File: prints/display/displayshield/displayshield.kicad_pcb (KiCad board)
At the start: 2 copper layers, 9 parts, among them J1 Conn_01x16, J2 Screw_Terminal_01x11, SW1 SW_Push

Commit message: Finished Displayshield Print
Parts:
- added G***: LOGO, logo:Skógahöf_S, F.Cu at (182.1, 113.7)
- moved BZ1 128.9 mm to (162.3, 113.7)
- moved D1 116.4 mm to (180.5, 79.7)
- moved J2 107.8 mm to (124.1, 115.2), turned to 90 degrees
- moved SW1 106.4 mm to (145.6, 112.2)
- moved J1 99.1 mm to (133.6, 79.7), turned to 90 degrees
- moved RV1 98.7 mm to (137.6, 113.6)
- moved R3 97.5 mm to (140.1, 109.7)
- moved R2 96.3 mm to (136.1, 109.7)
- moved R1 95.5 mm to (132.1, 109.7)
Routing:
- net GND: track 0.00 -> 157.5 mm
- net Net-(J2-Pin_9): track 0.00 -> 147.6 mm
- net +5V: track 0.00 -> 139.3 mm
- net Net-(BZ1-+): track 0.00 -> 103.4 mm
- net Net-(J1-Pin_14): track 0.00 -> 88.0 mm
- net Net-(J1-Pin_13): track 0.00 -> 77.7 mm
- net Net-(J1-Pin_12): track 0.00 -> 70.1 mm
- net Net-(J1-Pin_6): track 0.00 -> 69.7 mm
- net Net-(J1-Pin_11): track 0.00 -> 62.3 mm
- net Net-(J2-Pin_11): track 0.00 -> 59.1 mm
- net Net-(D1-A): track 0.00 -> 54.4 mm
- net Net-(J1-Pin_15): track 0.00 -> 50.5 mm
- net Net-(J1-Pin_3): track 0.00 -> 48.1 mm
- net Net-(J1-Pin_4): track 0.00 -> 24.9 mm
- net (no net): vias 0 -> 4
- added copper zone on B.Cu, net GND
- added copper zone on F.Cu, net GND
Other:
- board outline added: 80 x 52 mm
- board text added: "PREN2: Skógahöf DisplayShield"
- board text added: "Revision 1.0"

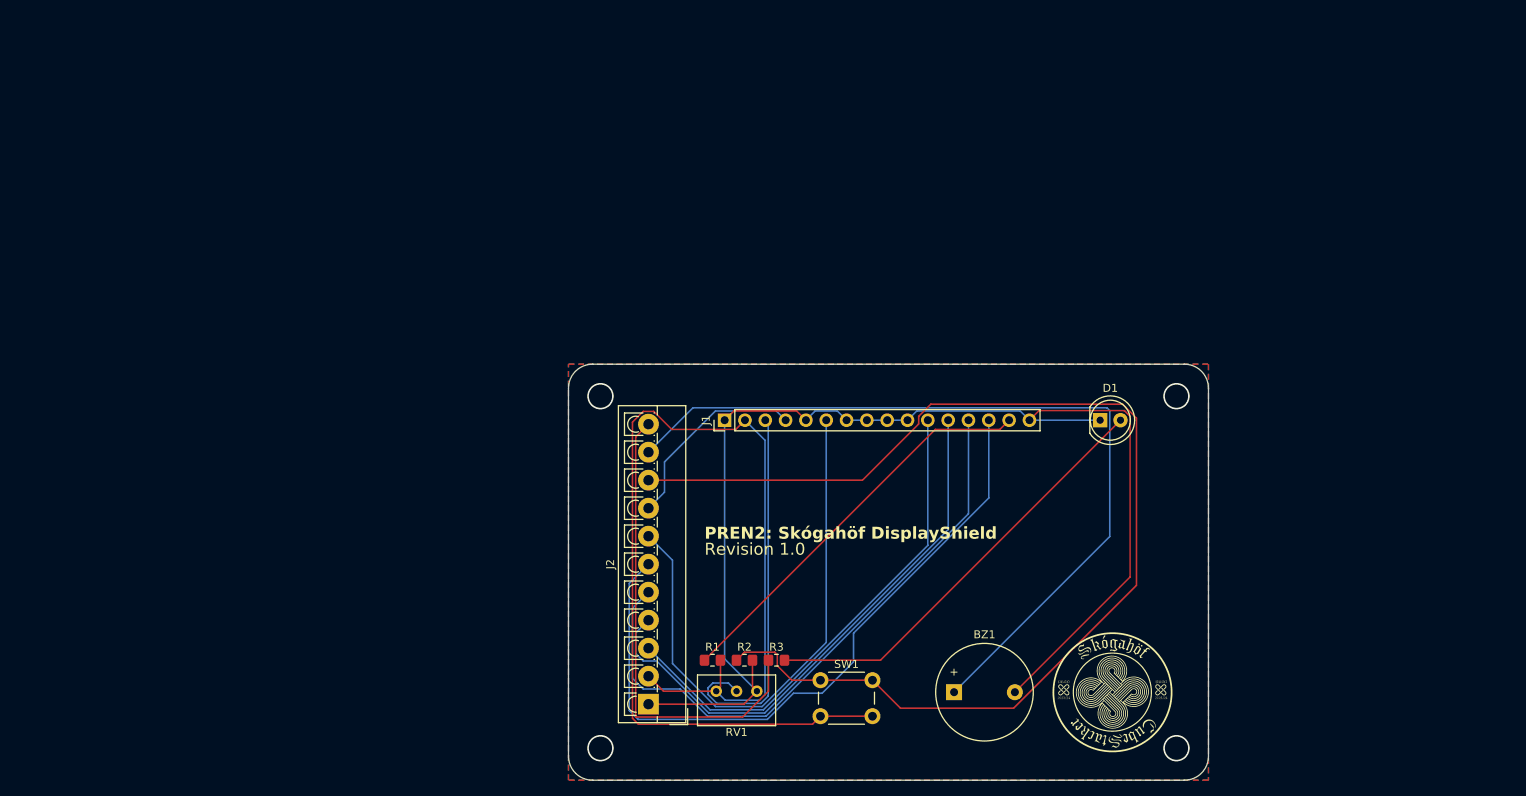
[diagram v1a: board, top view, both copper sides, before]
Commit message: added new Printfiles for Displayshield and Measurements for second stack
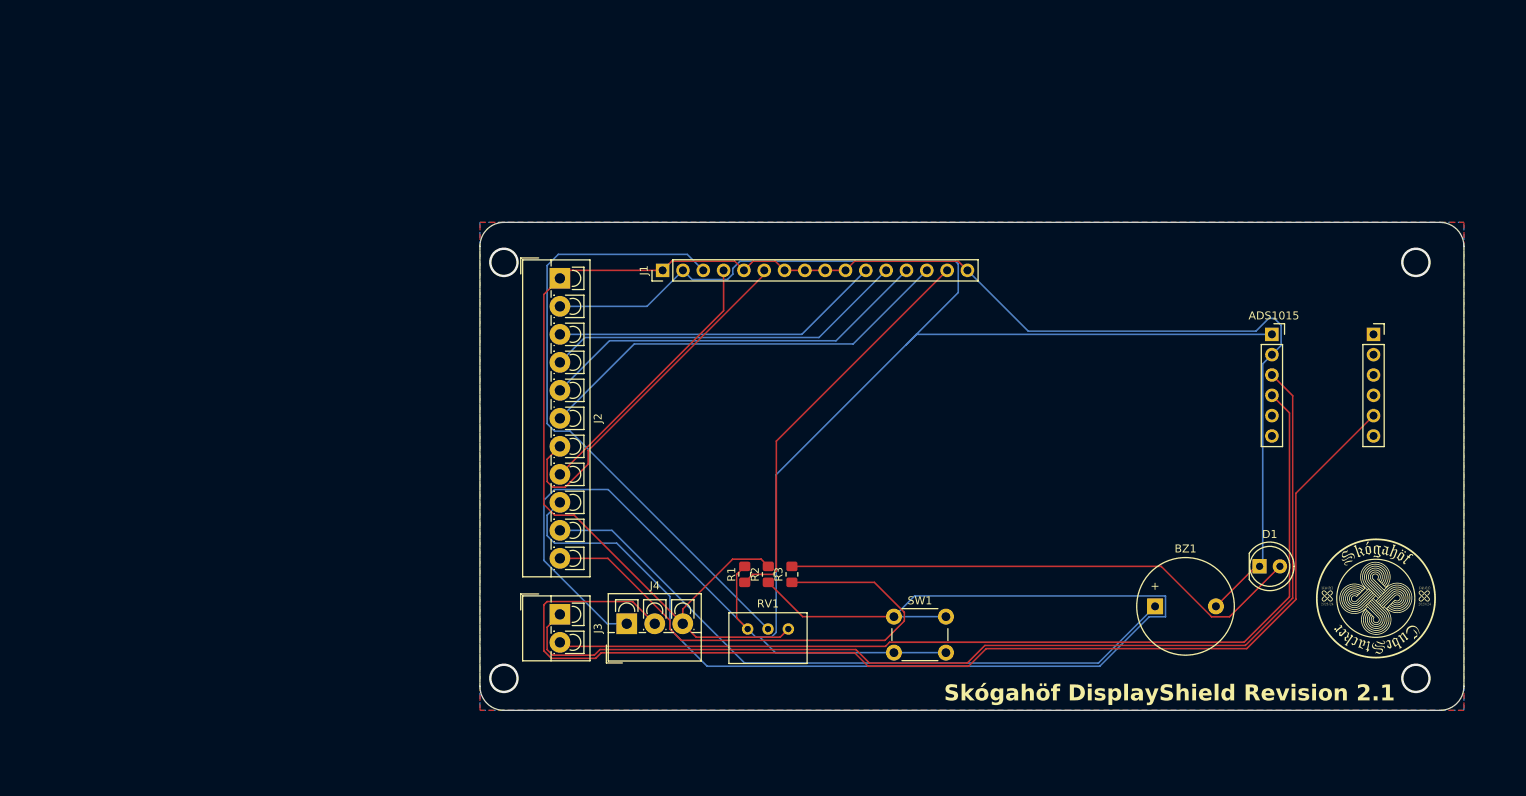
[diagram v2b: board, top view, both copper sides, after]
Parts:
- added ADS1015: ~, ADAFRUIT:ADS1015, F.Cu at (208.7, 73.2)
- added J3: RaspberryPiADC, TerminalBlock_4Ucon:TerminalBlock_4Ucon_1x02_P3.50mm_Vertical, F.Cu at (113.0, 104.0)
- added J4: CurrentSensor, TerminalBlock_4Ucon:TerminalBlock_4Ucon_1x03_P3.50mm_Vertical, F.Cu at (121.4, 105.2)
- J1: value Conn_01x16 -> Display
- J2: value Screw_Terminal_01x11 -> RaspberryPiDisplay
- moved J2 54.4 mm to (113.0, 62.0), turned to -90 degrees
- moved G*** 35.0 mm to (215.0, 102.0)
- moved BZ1 27.3 mm to (187.4, 103.0)
- moved D1 27.0 mm to (200.5, 98.0)
- moved J1 20.3 mm to (125.8, 61.0)
- moved SW1 12.1 mm to (154.8, 104.3)
- moved R1 11.5 mm to (136.1, 99.0), turned to 90 degrees
- moved R2 11.1 mm to (139.1, 99.0), turned to 90 degrees
- moved R3 10.9 mm to (142.0, 99.0), turned to 90 degrees
- moved RV1 8.71 mm to (141.6, 105.8)
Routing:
- net Net-(ADS1015-A0): track 0.00 -> 146.8 mm
- net Net-(ADS1015-SCL): track 0.00 -> 131.9 mm
- net Net-(ADS1015-SDA): track 0.00 -> 120.1 mm
- net +5V: track 139.3 -> 246.9 mm
- net GND: track 157.5 -> 218.8 mm
- net Net-(J1-Pin_14): track 88.0 -> 53.5 mm
- net Net-(J1-Pin_3): track 48.1 -> 78.9 mm
- net Net-(J1-Pin_13): track 77.7 -> 49.5 mm
- net Net-(J1-Pin_6): track 69.7 -> 45.0 mm
- net Net-(J1-Pin_12): track 70.1 -> 45.5 mm
- net Net-(J1-Pin_11): track 62.3 -> 41.6 mm
- net Net-(BZ1-+): track 103.4 -> 84.2 mm
- net Net-(D1-A): track 54.4 -> 66.2 mm
- net Net-(J1-Pin_4): track 24.9 -> 34.0 mm
- net Net-(J2-Pin_9): track 147.6 -> 155.4 mm
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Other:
- board size 80 x 52 mm -> 123 x 61 mm
- board text added: "Skógahöf DisplayShield Revision 2.1"
- board text removed: "PREN2: Skógahöf DisplayShield"
- board text removed: "Revision 1.0"

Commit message: updated StackMeasurements
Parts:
- moved ADS1015 2.69 mm to (211.4, 73.2)
- moved J2 2.69 mm to (115.7, 62.0)
- moved J3 2.69 mm to (115.7, 104.0)
- moved J4 2.69 mm to (124.0, 105.2)
- moved BZ1 2.69 mm to (190.1, 103.0)
- moved D1 2.69 mm to (203.2, 98.0)
- moved J1 2.69 mm to (128.5, 61.0)
- moved R1 2.69 mm to (138.8, 99.0)
- moved R2 2.69 mm to (141.7, 99.0)
- moved R3 2.69 mm to (144.7, 99.0)
- moved RV1 2.69 mm to (144.2, 105.8)
- moved SW1 2.69 mm to (157.4, 104.3)
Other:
- board size 123 x 61 mm -> 123 x 60 mm

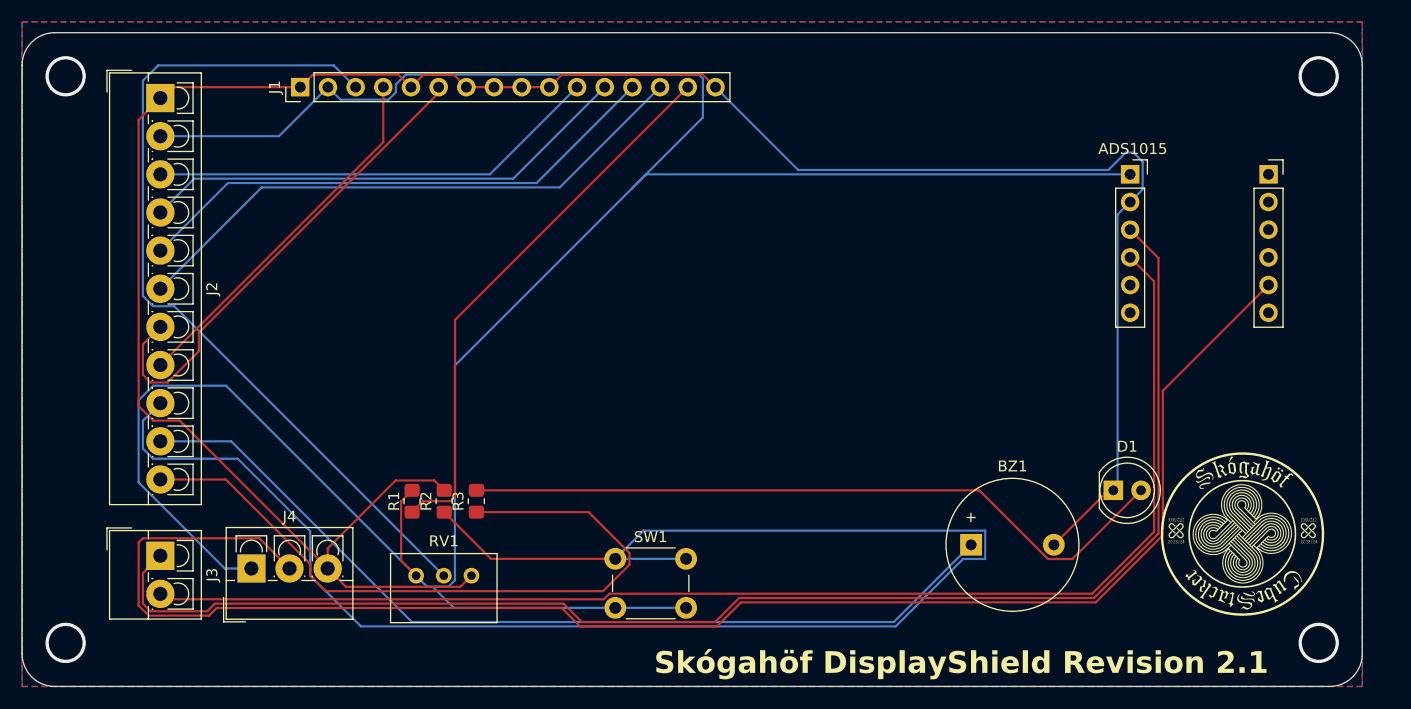
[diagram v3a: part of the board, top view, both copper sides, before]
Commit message: Prints for Hallsensor
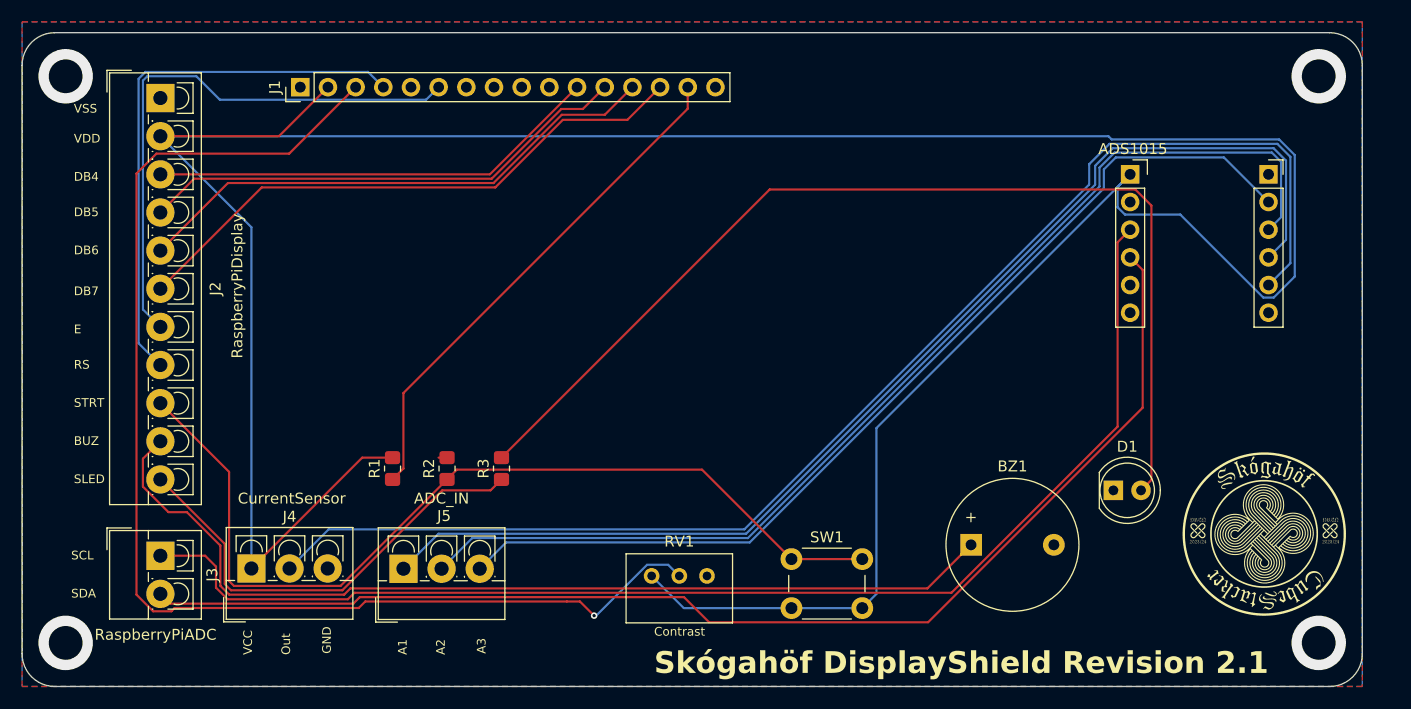
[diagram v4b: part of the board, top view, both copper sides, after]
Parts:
- added J5: ADC_IN, TerminalBlock_4Ucon:TerminalBlock_4Ucon_1x03_P3.50mm_Vertical, F.Cu at (138.0, 105.2)
- moved RV1 21.6 mm to (165.9, 105.9)
- moved SW1 16.2 mm to (173.6, 104.3)
- moved R3 3.78 mm to (147.0, 96.0)
- moved R1 3.49 mm to (137.0, 96.0)
- moved R2 3.01 mm to (142.0, 96.0)
- moved G*** 2.00 mm to (217.0, 102.0)
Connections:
- ADS1015 pad 10: unconnected-(ADS1015-A1-Pad10) -> Net-(ADS1015-A1)
- ADS1015 pad 8: unconnected-(ADS1015-A3-Pad8) -> Net-(ADS1015-A3)
- ADS1015 pad 9: unconnected-(ADS1015-A2-Pad9) -> Net-(ADS1015-A2)
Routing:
- net GND: track 218.8 -> 1.24 mm
- net Net-(ADS1015-A1): track 0.00 -> 108.0 mm
- net Net-(ADS1015-A2): track 0.00 -> 100.9 mm
- net Net-(ADS1015-A3): track 0.00 -> 90.7 mm
- net Net-(J2-Pin_9): track 155.4 -> 85.1 mm
- net +5V: track 246.9 -> 288.9 mm
- net Net-(J1-Pin_3): track 78.9 -> 115.8 mm, vias 0 -> 1
- net Net-(D1-A): track 66.2 -> 97.0 mm
- net Net-(ADS1015-A0): track 146.8 -> 122.2 mm
- net Net-(J2-Pin_11): track 65.6 -> 41.9 mm
- net Net-(J1-Pin_4): track 34.0 -> 50.4 mm
- net Net-(ADS1015-SCL): track 131.9 -> 115.7 mm
- net Net-(J1-Pin_6): track 45.0 -> 52.2 mm
- net Net-(ADS1015-SDA): track 120.1 -> 114.2 mm
- net Net-(BZ1-+): track 84.2 -> 89.0 mm
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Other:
- board text added: "A1"
- board text added: "A2"
- board text added: "A3"
- board text added: "BUZ"
- board text added: "Contrast"
- board text added: "DB4"
- board text added: "DB5"
- board text added: "DB6"
- board text added: "DB7"
- board text added: "E"
- board text added: "GND"
- board text added: "Out"
- board text added: "RS"
- board text added: "SCL"
- board text added: "SDA"
- board text added: "SLED"
- board text added: "STRT"
- board text added: "VCC"
- board text added: "VDD"
- board text added: "VSS"
